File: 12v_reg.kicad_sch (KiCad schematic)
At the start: 21 parts, among them U2 SiC467

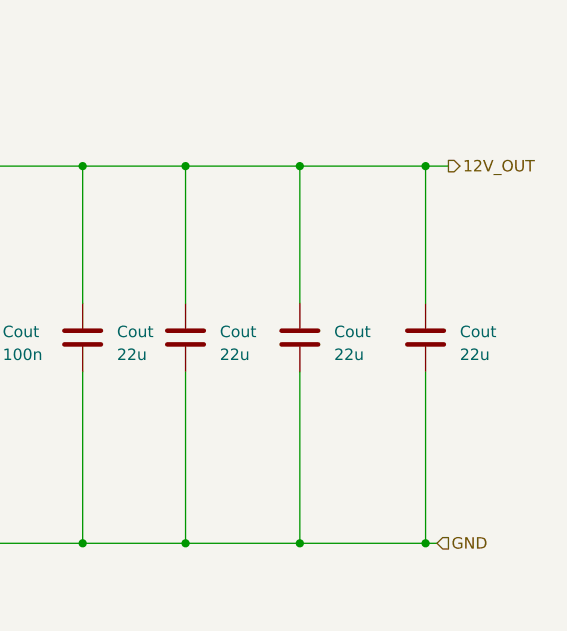
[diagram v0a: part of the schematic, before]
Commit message: Added connections to signal board, battery, and mounting holes
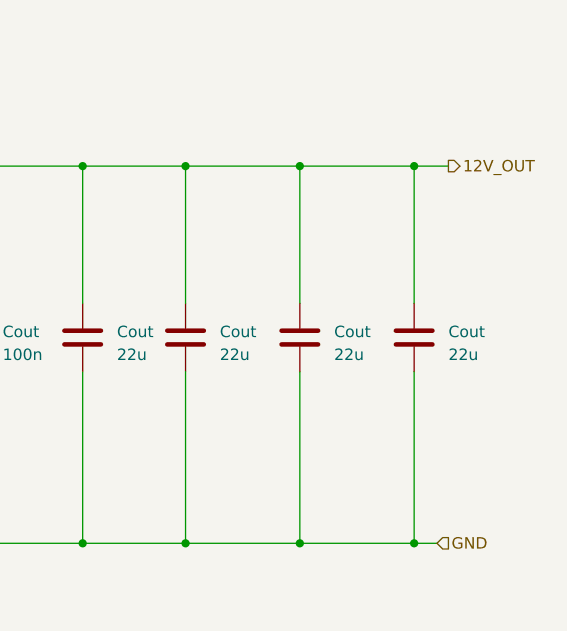
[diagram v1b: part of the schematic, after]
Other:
- moved on the sheet: Cout
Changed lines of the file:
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@@
 (kicad_sch (version 20230121) (generator eeschema)
   (paper "A4")
-  (junction (at 238.76 111.76) (diameter 0) (color 0 0 0 0)
-  )
   (junction (at 114.3 62.23) (diameter 0) (color 0 0 0 0)
   )
@@
   (junction (at 135.89 110.49) (diameter 0) (color 0 0 0 0)
   )
-  (junction (at 238.76 69.85) (diameter 0) (color 0 0 0 0)
-  )
   (junction (at 154.94 69.85) (diameter 0) (color 0 0 0 0)
   )
@@
   (junction (at 200.66 111.76) (diameter 0) (color 0 0 0 0)
   )
+  (junction (at 237.49 69.85) (diameter 0) (color 0 0 0 0)
+  )
   (junction (at 74.93 99.06) (diameter 0) (color 0 0 0 0)
   )
@@
   )
   (junction (at 110.49 74.93) (diameter 0) (color 0 0 0 0)
+  )
+  (junction (at 237.49 111.76) (diameter 0) (color 0 0 0 0)
   )
   (junction (at 187.96 69.85) (diameter 0) (color 0 0 0 0)
@@
   (no_connect (at 153.67 80.01))
   (no_connect (at 153.67 104.14))
-  (wire (pts (xy 238.76 69.85) (xy 241.3 69.85))
-    (stroke (width 0) (type default))
-  )
-  (wire (pts (xy 238.76 111.76) (xy 240.03 111.76))
+  (wire (pts (xy 237.49 111.76) (xy 240.03 111.76))
     (stroke (width 0) (type default))
   )
@@
     (stroke (width 0) (type default))
   )
-  (wire (pts (xy 224.79 69.85) (xy 238.76 69.85))
+  (wire (pts (xy 224.79 69.85) (xy 237.49 69.85))
     (stroke (width 0) (type default))
   )
@@
     (stroke (width 0) (type default))
   )
+  (wire (pts (xy 237.49 69.85) (xy 241.3 69.85))
+    (stroke (width 0) (type default))
+  )
   (wire (pts (xy 99.06 110.49) (xy 99.06 111.76))
     (stroke (width 0) (type default))
@@
     (stroke (width 0) (type default))
   )
-  (wire (pts (xy 238.76 92.71) (xy 238.76 111.76))
+  (wire (pts (xy 237.49 92.71) (xy 237.49 111.76))
     (stroke (width 0) (type default))
   )
@@
     (stroke (width 0) (type default))
   )
-  (wire (pts (xy 238.76 69.85) (xy 238.76 85.09))
+  (wire (pts (xy 237.49 69.85) (xy 237.49 85.09))
     (stroke (width 0) (type default))
   )
@@
     (stroke (width 0) (type default))
   )
-  (wire (pts (xy 224.79 111.76) (xy 238.76 111.76))
+  (wire (pts (xy 224.79 111.76) (xy 237.49 111.76))
     (stroke (width 0) (type default))
   )
@@
     )
   )
-  (symbol (lib_id "Device:C") (at 238.76 88.9 0) (unit 1)
+  (symbol (lib_id "Device:C") (at 237.49 88.9 0) (unit 1)
     (in_bom yes) (on_board yes) (dnp no) (fields_autoplaced)
-    (property "Reference" "Cout" (at 242.57 88.265 0)
+    (property "Reference" "Cout" (at 241.3 88.265 0)
       (effects (font (size 1.27 1.27)) (justify left))
     )
-    (property "Value" "22u" (at 242.57 90.805 0)
+    (property "Value" "22u" (at 241.3 90.805 0)
       (effects (font (size 1.27 1.27)) (justify left))
     )
-    (property "Footprint" "Capacitor_SMD:C_1210_3225Metric" (at 239.7252 92.71 0)
-      (effects (font (size 1.27 1.27)) hide)
-    )
-    (property "Datasheet" "~" (at 238.76 88.9 0)
-      (effects (font (size 1.27 1.27)) hide)
-    )
+    (property "Footprint" "Capacitor_SMD:C_1210_3225Metric" (at 238.4552 92.71 0)
+      (effects (font (size 1.27 1.27)) hide)
+    )
+    (property "Datasheet" "~" (at 237.49 88.9 0)
+      (effects (font (size 1.27 1.27)) hide)
+    )

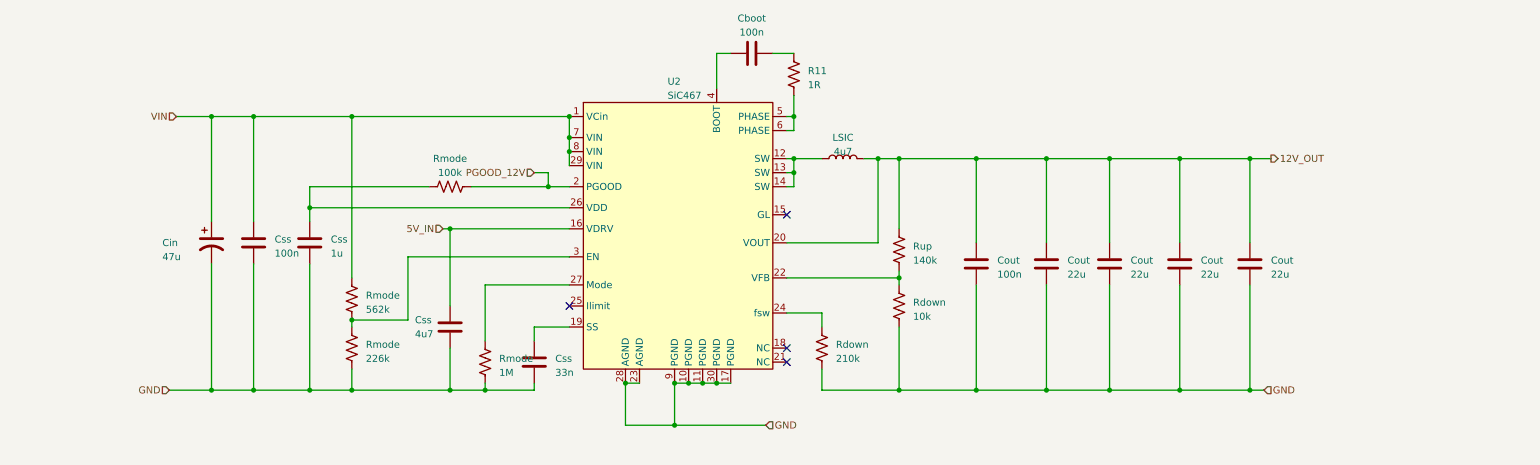
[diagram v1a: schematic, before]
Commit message: Changed 5V regulator and 12V regulator to the SiC461. Both support 10A and 5V and 12V respectively
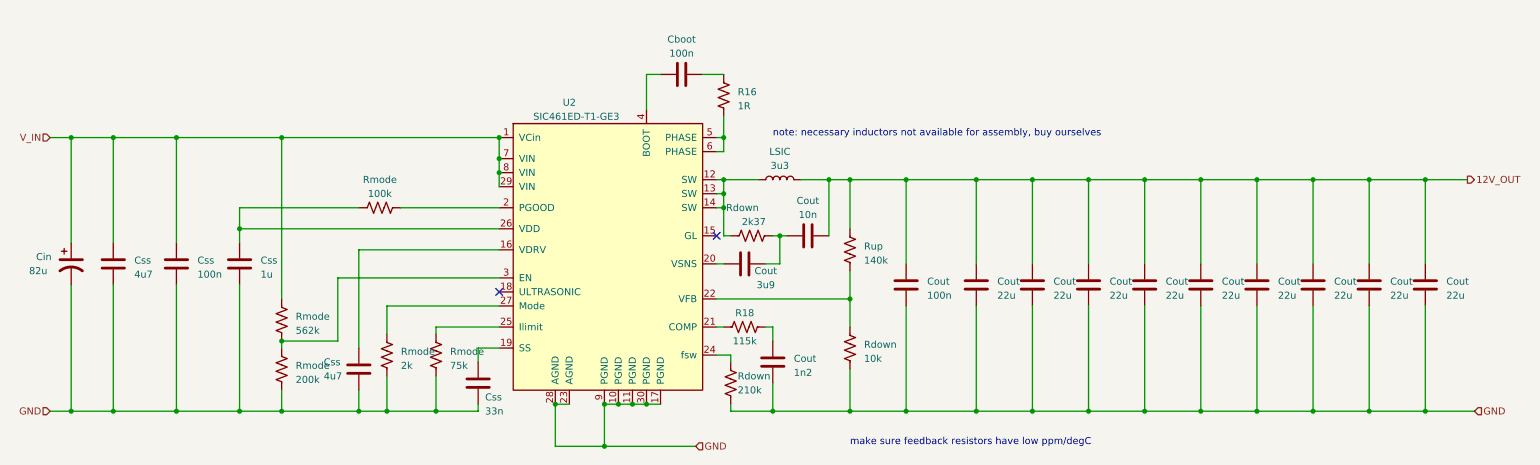
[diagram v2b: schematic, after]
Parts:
- removed U2: SiC467, crush-power-footprints:SIC467ED-T1-GE3, symbol crush-power-lib:SiC46x
- added Cout (x5): 22u, Capacitor_SMD:C_1210_3225Metric, symbol Device:C
- added Cout: 3u9, Capacitor_SMD:C_0402_1005Metric, symbol Device:C
- added Cout: 1n2, Capacitor_SMD:C_0603_1608Metric, symbol Device:C
- added Cout: 10n, Capacitor_SMD:C_0402_1005Metric, symbol Device:C
- added Css: 4u7, Capacitor_SMD:C_0603_1608Metric, symbol Device:C
- added R18: 115k, Resistor_SMD:R_0402_1005Metric, symbol Device:R_US
- added Rdown: 2k37, Resistor_SMD:R_0402_1005Metric, symbol Device:R_US
- added Rmode: 75k, Resistor_SMD:R_0603_1608Metric, symbol Device:R_US
- added U2: SIC461ED-T1-GE3, crush-power-footprints:CONV_SIC461ED-T1-GE3, symbol crush-power-lib:SIC461ED-T1-GE3
- Cin: value 47u -> 82u
- Css: footprint Capacitor_SMD:C_0603_1608Metric -> Capacitor_SMD:C_0805_2012Metric
- LSIC: value 4u7 -> 3u3
- Rmode: value 1M -> 2k
- Rmode: value 226k -> 200k
- renumbered R11 to R16
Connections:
- net 12V_OUT: now also Cout.1, Cout.1, Cout.1, Cout.1, Cout.1, Cout.2
- net GND: now also Cout.2, Cout.2, Cout.2, Cout.2, Cout.2, Cout.2, Css.1, Rmode.2, U2.10 (PGND), U2.11 (PGND), U2.17 (PGND), U2.23 (AGND), U2.28 (AGND), U2.30 (PGND), U2.9 (PGND)
- net at R16.1: now also U2.5 (PHASE), U2.6 (PHASE)
- net at Css.2: now also U2.19 (SS)
- net at Cboot.1: now also U2.4 (BOOT)
- net at Css.2, Rmode.1: now also U2.26 (VDD)
- net at LSIC.1: now also Rdown.1, U2.12 (SW), U2.13 (SW), U2.14 (SW)
- net at Rdown.1, Rup.2: now also U2.22 (VFB)
- net at Rdown.1: now also U2.24 (fsw)
- net at Rmode.1: now also U2.27 (Mode)
- net at Rmode.1, Rmode.2: now also U2.3 (EN)
- net 5V_IN: no longer names the net of Css.2
- net 5V_IN: now also U2.16 (VDRV)
- net PGOOD_12V: no longer names the net of Rmode.2
- net PGOOD_12V: now also U2.2 (PGOOD)
- net VIN renamed V_IN
- net V_IN: now also Css.2, U2.1 (VCin), U2.29 (VIN), U2.7 (VIN), U2.8 (VIN)
- new net: Cout.1, U2.20 (VSNS)
- new net: Cout.1, Cout.2, Rdown.2
- new net: R18.1, U2.21 (COMP)
- new net: Cout.1, R18.2
- new net: Rmode.1, U2.25 (Ilimit)
- no-connect marks 4 -> 2
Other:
- note added: "make sure feedback resistors have low ppm/degC"
- note added: "note: necessary inductors not available for assembly, buy ourselves"
- moved on the sheet: Cboot, Cin, Cout, Css, LSIC, R16, Rdown, Rmode, Rup

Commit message: Added more to the layout of the 12V regulator as well as changed some capacitor footprints
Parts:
- Cin: footprint Capacitor_Tantalum_SMD:CP_EIA-7343-15_Kemet-W -> Capacitor_THT:CP_Radial_D8.0mm_P3.50mm
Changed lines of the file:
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@@
       (effects (font (size 1.27 1.27)) (justify left))
     )
-    (property "Footprint" "Capacitor_Tantalum_SMD:CP_EIA-7343-15_Kemet-W" (at 24.13 88.9 0)
+    (property "Footprint" "Capacitor_THT:CP_Radial_D8.0mm_P3.50mm" (at 24.13 88.9 0)
       (effects (font (size 1.27 1.27)) hide)
     )
@@
       (effects (font (size 1.27 1.27)) (justify bottom) hide)
     )
-    (property "Datasheet" "" (at 120.65 88.9 0)
+    (property "Datasheet" "https://datasheet.lcsc.com/lcsc/2003271205_Vishay-Intertech-SIC461ED-T1-GE3_C499531.pdf" (at 120.65 88.9 0)
       (effects (font (size 1.27 1.27)) hide)
     )

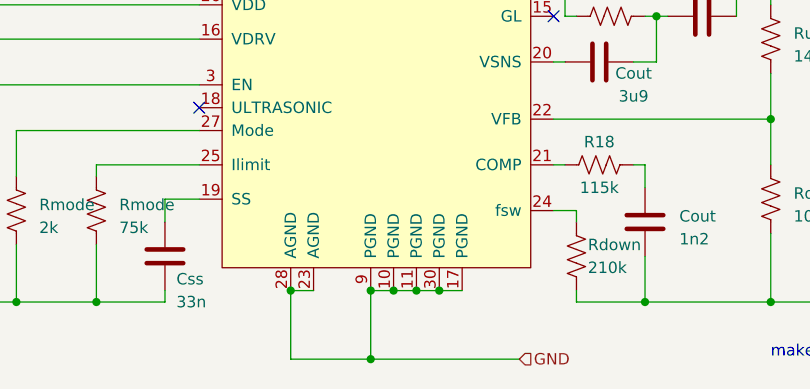
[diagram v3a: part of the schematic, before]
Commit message: Added thermal vias to the 12V regulator, fixed GND pad nets on 12V and 5V regulator
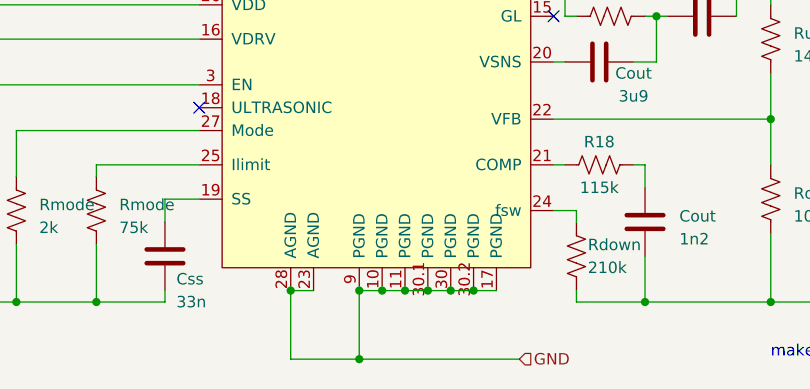
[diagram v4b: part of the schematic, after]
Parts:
- U2: footprint crush-power-footprints:CONV_SIC461ED-T1-GE3 -> CONV_SIC461ED-T1-GE3
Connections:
- net GND: now also U2.30.1 (PGND), U2.30.2 (PGND)
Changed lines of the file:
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@@
   (junction (at 248.92 73.66) (diameter 0) (color 0 0 0 0)
   )
+  (junction (at 119.38 121.92) (diameter 0) (color 0 0 0 0)
+  )
   (junction (at 259.08 73.66) (diameter 0) (color 0 0 0 0)
   )
@@
   (junction (at 54.61 115.57) (diameter 0) (color 0 0 0 0)
   )
-  (junction (at 120.65 121.92) (diameter 0) (color 0 0 0 0)
-  )
   (junction (at 218.44 73.66) (diameter 0) (color 0 0 0 0)
   )
   (junction (at 101.6 69.85) (diameter 0) (color 0 0 0 0)
   )
-  (junction (at 128.27 114.3) (diameter 0) (color 0 0 0 0)
-  )
   (junction (at 76.2 115.57) (diameter 0) (color 0 0 0 0)
   )
@@
   (junction (at 43.18 115.57) (diameter 0) (color 0 0 0 0)
   )
+  (junction (at 129.54 114.3) (diameter 0) (color 0 0 0 0)
+  )
+  (junction (at 121.92 114.3) (diameter 0) (color 0 0 0 0)
+  )
   (junction (at 198.12 115.57) (diameter 0) (color 0 0 0 0)
   )
   (junction (at 152.4 83.82) (diameter 0) (color 0 0 0 0)
   )
-  (junction (at 123.19 114.3) (diameter 0) (color 0 0 0 0)
+  (junction (at 132.08 114.3) (diameter 0) (color 0 0 0 0)
   )
   (junction (at 198.12 73.66) (diameter 0) (color 0 0 0 0)
@@
   (junction (at 238.76 115.57) (diameter 0) (color 0 0 0 0)
   )
+  (junction (at 127 114.3) (diameter 0) (color 0 0 0 0)
+  )
   (junction (at 54.61 82.55) (diameter 0) (color 0 0 0 0)
   )
@@
   (junction (at 142.24 66.04) (diameter 0) (color 0 0 0 0)
   )
+  (junction (at 119.38 114.3) (diameter 0) (color 0 0 0 0)
+  )
   (junction (at 187.96 115.57) (diameter 0) (color 0 0 0 0)
   )
@@
   (junction (at 165.1 115.57) (diameter 0) (color 0 0 0 0)
   )
-  (junction (at 120.65 114.3) (diameter 0) (color 0 0 0 0)
-  )
   (junction (at 142.24 76.2) (diameter 0) (color 0 0 0 0)
   )
@@
   (junction (at 62.23 115.57) (diameter 0) (color 0 0 0 0)
   )
+  (junction (at 124.46 114.3) (diameter 0) (color 0 0 0 0)
+  )
   (junction (at 101.6 66.04) (diameter 0) (color 0 0 0 0)
-  )
-  (junction (at 125.73 114.3) (diameter 0) (color 0 0 0 0)
   )
   (no_connect (at 101.6 93.98))
@@
     (stroke (width 0) (type default))
   )
-  (wire (pts (xy 125.73 114.3) (xy 128.27 114.3))
-    (stroke (width 0) (type default))
-  )
   (wire (pts (xy 140.97 73.66) (xy 142.24 73.66))
     (stroke (width 0) (type default))
@@
     (stroke (width 0) (type default))
   )
-  (wire (pts (xy 128.27 114.3) (xy 130.81 114.3))
-    (stroke (width 0) (type default))
-  )
   (wire (pts (xy 72.39 102.87) (xy 62.23 102.87))
     (stroke (width 0) (type default))
@@
     (stroke (width 0) (type default))
   )
-  (wire (pts (xy 120.65 114.3) (xy 123.19 114.3))
+  (wire (pts (xy 121.92 114.3) (xy 124.46 114.3))
     (stroke (width 0) (type default))
   )
@@
     (stroke (width 0) (type default))
   )
-  (wire (pts (xy 111.76 121.92) (xy 120.65 121.92))
-    (stroke (width 0) (type default))
-  )
-  (wire (pts (xy 120.65 121.92) (xy 137.16 121.92))
+  (wire (pts (xy 111.76 121.92) (xy 119.38 121.92))
     (stroke (width 0) (type default))
   )
@@
     (stroke (width 0) (type default))
   )
+  (wire (pts (xy 132.08 114.3) (xy 134.62 114.3))
+    (stroke (width 0) (type default))
+  )
   (wire (pts (xy 111.76 114.3) (xy 111.76 121.92))
     (stroke (width 0) (type default))
@@
     (stroke (width 0) (type default))
   )
+  (wire (pts (xy 127 114.3) (xy 129.54 114.3))
+    (stroke (width 0) (type default))
+  )
   (wire (pts (xy 151.13 100.33) (xy 151.13 102.87))
     (stroke (width 0) (type default))
@@
     (stroke (width 0) (type default))
   )
+  (wire (pts (xy 129.54 114.3) (xy 132.08 114.3))
+    (stroke (width 0) (type default))
+  )
   (wire (pts (xy 218.44 115.57) (xy 228.6 115.57))
     (stroke (width 0) (type default))
@@
     (stroke (width 0) (type default))
   )
+  (wire (pts (xy 119.38 121.92) (xy 137.16 121.92))
+    (stroke (width 0) (type default))
+  )
   (wire (pts (xy 54.61 92.71) (xy 54.61 115.57))
     (stroke (width 0) (type default))
@@
     (stroke (width 0) (type default))
   )
+  (wire (pts (xy 119.38 114.3) (xy 121.92 114.3))
+    (stroke (width 0) (type default))
+  )
   (wire (pts (xy 152.4 83.82) (xy 153.67 83.82))
     (stroke (width 0) (type default))
@@
     (stroke (width 0) (type default))
   )
-  (wire (pts (xy 123.19 114.3) (xy 125.73 114.3))
-    (stroke (width 0) (type default))
-  )
   (wire (pts (xy 142.24 62.23) (xy 142.24 66.04))
     (stroke (width 0) (type default))
@@
     (stroke (width 0) (type default))
   )
+  (wire (pts (xy 124.46 114.3) (xy 127 114.3))
+    (stroke (width 0) (type default))
+  )
   (wire (pts (xy 138.43 54.61) (xy 142.24 54.61))
     (stroke (width 0) (type default))
@@
     (stroke (width 0) (type default))
   )
-  (wire (pts (xy 120.65 114.3) (xy 120.65 121.92))
+  (wire (pts (xy 119.38 114.3) (xy 119.38 121.92))
     (stroke (width 0) (type default))
   )
@@
       (effects (font (size 1.27 1.27)))
     )
-    (property "Footprint" "crush-power-footprints:CONV_SIC461ED-T1-GE3" (at 120.65 88.9 0)
+    (property "Footprint" "CONV_SIC461ED-T1-GE3" (at 120.65 88.9 0)
       (effects (font (size 1.27 1.27)) (justify bottom) hide)
     )
@@
     (pin "3")
     (pin "30")
+    (pin "30.1")
+    (pin "30.2")
     (pin "4")
     (pin "5")

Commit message: fix batt_t planes
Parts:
- renumbered Css to C10, Cboot to C11, Cout to C12, Cout to C13, Cout to C14, Cout to C15, Cout to C16, Cout to C17, Cout to C18, Cout to C19, Cout to C20, Cout to C21, Cout to C22, Cout to C23, Cout to C24, Cin to C5, Css to C6, Css to C7, Css to C8, Css to C9, LSIC to L2, Rmode to R11, Rmode to R12, Rmode to R13, Rmode to R14, Rmode to R15, Rdown to R17, Rdown to R19, Rup to R20, Rdown to R21

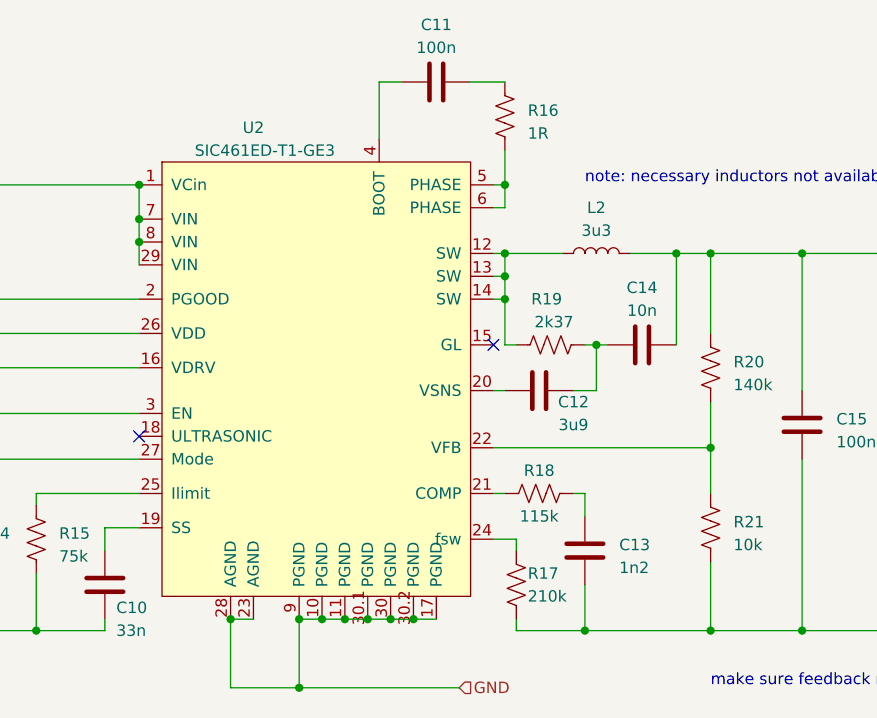
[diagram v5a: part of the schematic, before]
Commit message: drc fixes and update schematic to reflect correct ic footprints
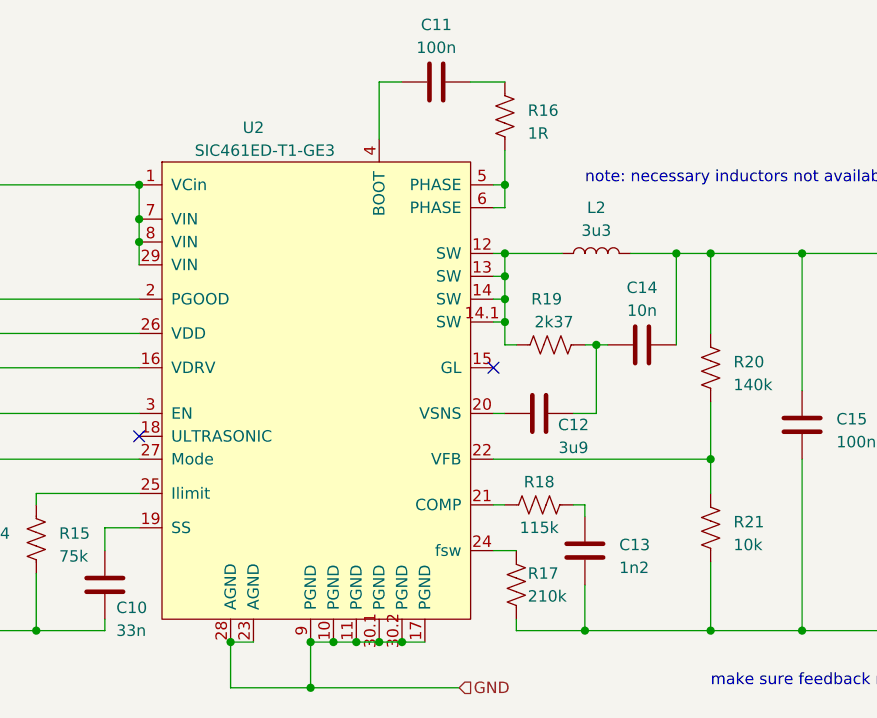
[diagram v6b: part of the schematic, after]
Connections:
- net GND: no longer U2.30 (PGND)
- net at L2.1, R19.1, U2.12 (SW)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: now also U2.14.1 (SW)
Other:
- moved on the sheet: C12, R18, U2

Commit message: use 4u7 capacitors for vsns pins
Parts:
- C12: value 3u9 -> 4u7; footprint Capacitor_SMD:C_0402_1005Metric -> Capacitor_SMD:C_0805_2012Metric
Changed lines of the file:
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@@
       (effects (font (size 1.27 1.27)))
     )
-    (property "Value" "3u9" (at 149.86 95.25 90)
+    (property "Value" "4u7" (at 149.86 95.25 90)
       (effects (font (size 1.27 1.27)))
     )
-    (property "Footprint" "Capacitor_SMD:C_0402_1005Metric" (at 149.86 90.4748 0)
+    (property "Footprint" "Capacitor_SMD:C_0805_2012Metric" (at 149.86 90.4748 0)
       (effects (font (size 1.27 1.27)) hide)
     )
